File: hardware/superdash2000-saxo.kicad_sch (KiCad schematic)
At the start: 8 parts, among them J1 Molex 34691-0161, U1 L7805

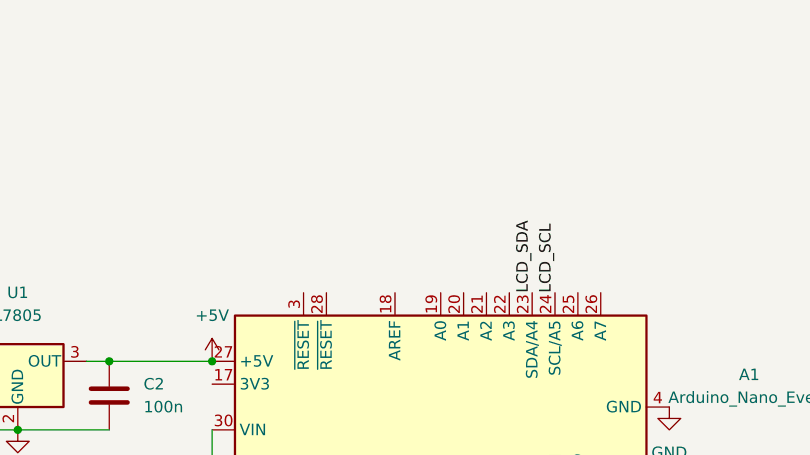
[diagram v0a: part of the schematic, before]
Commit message: hardware: Add voltage divider for battery measurement
Signed-off-by: Thomas Antonini <antonini.thomas@gmail.com>
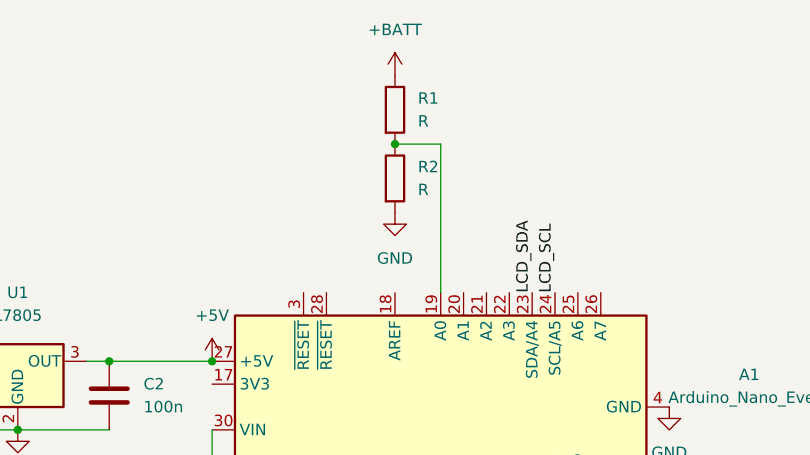
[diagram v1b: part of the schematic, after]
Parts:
- added R1, R2: R, symbol Device:R
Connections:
- net +BATT: now also R1.1
- net GND: now also R2.2
- net at A1.19 (A0): now also R1.2, R2.1
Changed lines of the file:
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@@
   (junction (at 123.19 58.42) (diameter 0) (color 0 0 0 0)
   )
+  (junction (at 154.94 34.29) (diameter 0) (color 0 0 0 0)
+  )
   (junction (at 113.03 66.04) (diameter 0) (color 0 0 0 0)
   )
@@
     (stroke (width 0) (type default) (color 0 0 0 0))
   )
+  (wire (pts (xy 160.02 34.29) (xy 154.94 34.29))
+    (stroke (width 0) (type default) (color 0 0 0 0))
+  )
   (wire (pts (xy 134.62 66.04) (xy 134.62 74.93))
     (stroke (width 0) (type default) (color 0 0 0 0))
@@
   )
   (wire (pts (xy 87.63 71.12) (xy 87.63 74.93))
+    (stroke (width 0) (type default) (color 0 0 0 0))
+  )
+  (wire (pts (xy 160.02 50.8) (xy 160.02 34.29))
     (stroke (width 0) (type default) (color 0 0 0 0))
   )
@@
     )
     (property "Datasheet" "" (id 3) (at 38.1 64.77 0)
+      (effects (font (size 1.27 1.27)) hide)
+    )
+    (pin "1")
+  )
+  (symbol (lib_name "GND_1") (lib_id "power:GND") (at 154.94 41.91 0) (unit 1)
+    (in_bom yes) (on_board yes) (fields_autoplaced)
+    (property "Reference" "#PWR?" (id 0) (at 154.94 48.26 0)
+      (effects (font (size 1.27 1.27)) hide)
+    )
+    (property "Value" "GND" (id 1) (at 154.94 46.99 0))
+    (property "Footprint" "" (id 2) (at 154.94 41.91 0)
+      (effects (font (size 1.27 1.27)) hide)
+    )
+    (property "Datasheet" "" (id 3) (at 154.94 41.91 0)
       (effects (font (size 1.27 1.27)) hide)
     )
@@
     (pin "3")
   )
+  (symbol (lib_id "power:+BATT") (at 154.94 26.67 0) (unit 1)
+    (in_bom yes) (on_board yes) (fields_autoplaced)
+    (property "Reference" "#PWR1" (id 0) (at 154.94 30.48 0)
+      (effects (font (size 1.27 1.27)) hide)
+    )
+    (property "Value" "+BATT" (id 1) (at 154.94 21.59 0))
+    (property "Footprint" "" (id 2) (at 154.94 26.67 0)
+      (effects (font (size 1.27 1.27)) hide)
+    )
+    (property "Datasheet" "" (id 3) (at 154.94 26.67 0)
+      (effects (font (size 1.27 1.27)) hide)
+    )
+    (pin "1")
+  )
   (symbol (lib_id "power:+BATT") (at 81.28 64.77 0) (unit 1)
     (in_bom yes) (on_board yes) (fields_autoplaced)
@@
     (pin "2")
   )
+  (symbol (lib_id "Device:R") (at 154.94 30.48 0) (unit 1)
+    (in_bom yes) (on_board yes) (fields_autoplaced)
+    (property "Reference" "R1" (id 0) (at 157.48 29.2099 0)
+      (effects (font (size 1.27 1.27)) (justify left))
+    )
+    (property "Value" "R" (id 1) (at 157.48 31.7499 0)
+      (effects (font (size 1.27 1.27)) (justify left))
+    )
+    (property "Footprint" "" (id 2) (at 153.162 30.48 90)
+      (effects (font (size 1.27 1.27)) hide)
+    )
+    (property "Datasheet" "~" (id 3) (at 154.94 30.48 0)
+      (effects (font (size 1.27 1.27)) hide)
+    )
+    (pin "1")
+    (pin "2")
+  )
+  (symbol (lib_id "Device:R") (at 154.94 38.1 0) (unit 1)
+    (in_bom yes) (on_board yes) (fields_autoplaced)
+    (property "Reference" "R2" (id 0) (at 157.48 36.8299 0)
+      (effects (font (size 1.27 1.27)) (justify left))
+    )
+    (property "Value" "R" (id 1) (at 157.48 39.3699 0)
+      (effects (font (size 1.27 1.27)) (justify left))
+    )
+    (property "Footprint" "" (id 2) (at 153.162 38.1 90)
+      (effects (font (size 1.27 1.27)) hide)
+    )
+    (property "Datasheet" "~" (id 3) (at 154.94 38.1 0)
+      (effects (font (size 1.27 1.27)) hide)
+    )
+    (pin "1")
+    (pin "2")
+  )
   (sheet_instances
     (path "/" (page "1"))
   )
   (symbol_instances
+    (path "/b87c930c-8d22-4000-a82f-ac742bad5f6a"
+      (reference "#PWR1") (unit 1) (value "+BATT") (footprint "")
+    )
     (path "/bfcc77a0-ee67-4af0-9e4b-c64f7ccc8208"
       (reference "#PWR1") (unit 1) (value "+BATT") (footprint "")
@@
       (reference "#PWR0106") (unit 1) (value "GND") (footprint "")
     )
+    (path "/2c2c0160-d229-41a2-b822-4cf1420ec8e9"
+      (reference "#PWR?") (unit 1) (value "GND") (footprint "")
+    )
     (path "/65c02b6a-4170-4a63-9193-eec01920d5e8"
       (reference "A1") (unit 1) (value "Arduino_Nano_Every") (footprint "Module:Arduino_Nano")
@@
       (reference "JP1") (unit 1) (value "Jumper_3_Bridged12") (footprint "")
     )
+    (path "/f89ebb12-89cc-4956-9979-cdeb115f9256"
+      (reference "R1") (unit 1) (value "R") (footprint "")
+    )
+    (path "/fece9861-2ca2-4e20-aacd-7057d18618e8"
+      (reference "R2") (unit 1) (value "R") (footprint "")
+    )
     (path "/8f188f22-a5b9-4f36-a20f-c9a07bb49266"

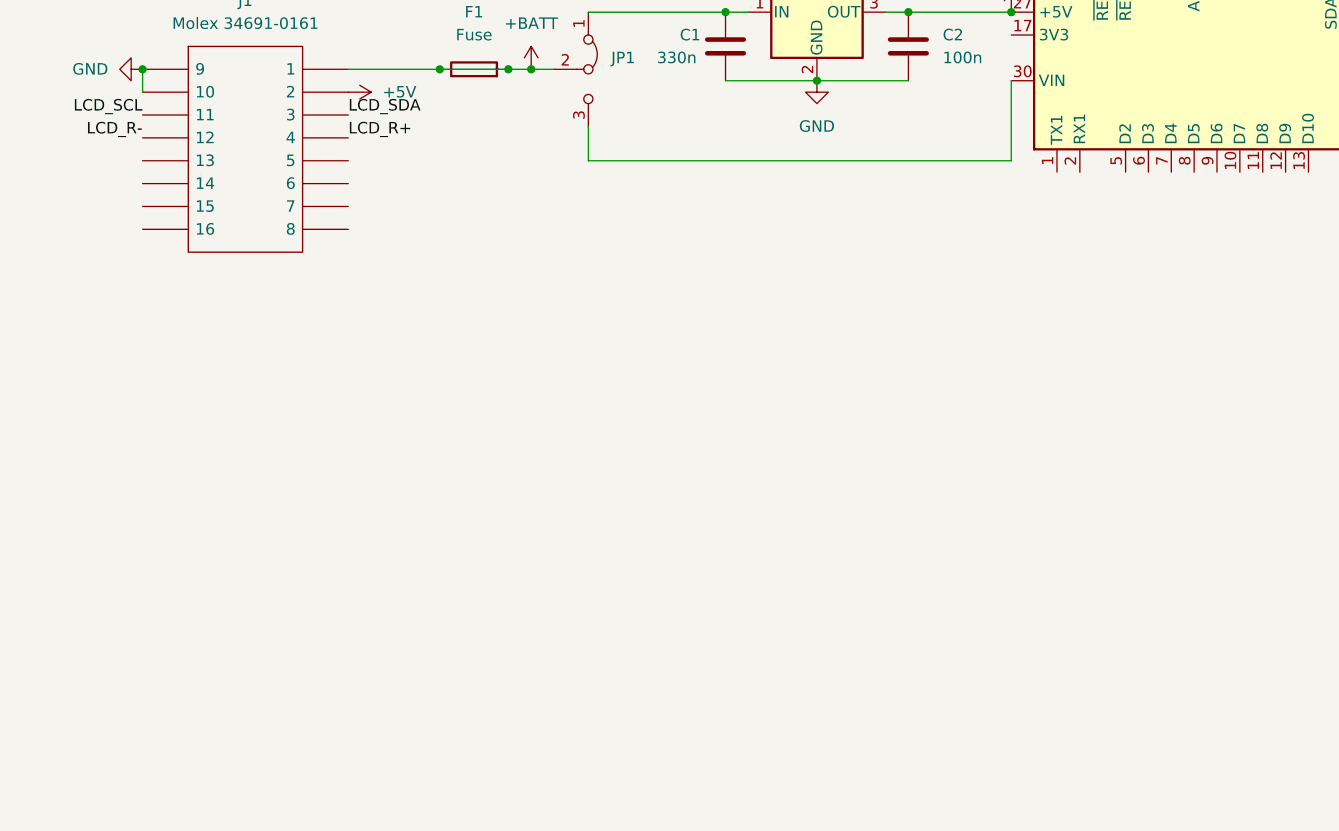
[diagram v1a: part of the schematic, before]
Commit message: hardware: Add water temp signal with opamp + voltage divider
Signed-off-by: Thomas Antonini <antonini.thomas@gmail.com>
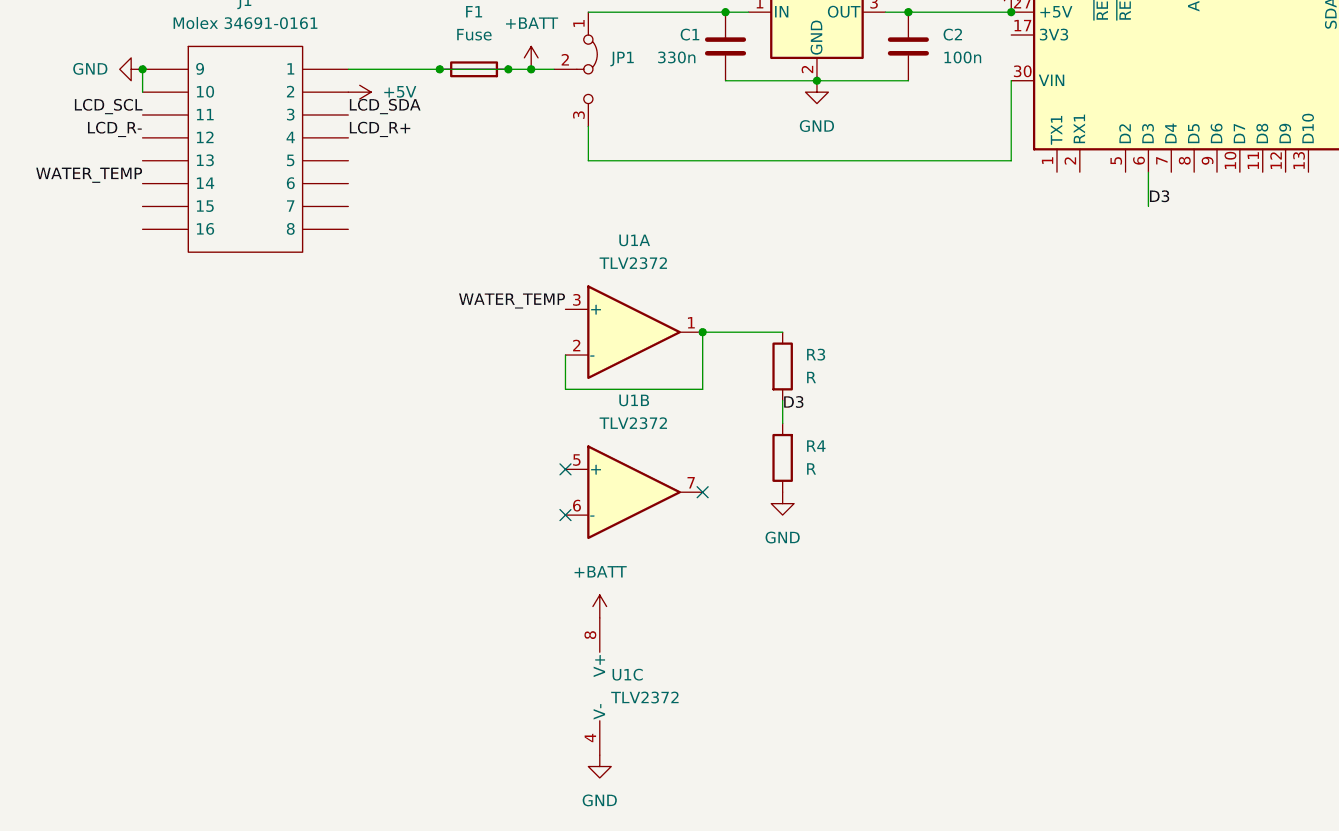
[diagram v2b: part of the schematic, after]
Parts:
- added R3, R4: R, symbol Device:R
- added unit 3 of U1
- added unit 2 of U1
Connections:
- net +BATT: now also U1.8 (V+)
- net GND: now also R4.1, U1.4 (V-)
- net D3: now reaches A1.6 (D3)
- net D3: now also R3.2, R4.2
- net WATER_TEMP: now reaches J1.14
- net WATER_TEMP: now also U1.3 (+)
- new net: R3.1, U1.1, U1.2 (-)
- no-connect marks 0 -> 3
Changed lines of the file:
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@@
   (junction (at 134.62 58.42) (diameter 0) (color 0 0 0 0)
   )
+  (junction (at 100.33 93.98) (diameter 0) (color 0 0 0 0)
+  )
   (junction (at 123.19 58.42) (diameter 0) (color 0 0 0 0)
   )
@@
   (junction (at 78.74 64.77) (diameter 0) (color 0 0 0 0)
   )
+  (no_connect (at 85.09 109.22))
+  (no_connect (at 85.09 114.3))
+  (no_connect (at 100.33 111.76))
   (wire (pts (xy 134.62 74.93) (xy 87.63 74.93))
     (stroke (width 0) (type default) (color 0 0 0 0))
@@
     (stroke (width 0) (type default) (color 0 0 0 0))
   )
+  (wire (pts (xy 85.09 100.33) (xy 100.33 100.33))
+    (stroke (width 0) (type default) (color 0 0 0 0))
+  )
+  (wire (pts (xy 85.09 96.52) (xy 85.09 100.33))
+    (stroke (width 0) (type default) (color 0 0 0 0))
+  )
+  (wire (pts (xy 149.86 76.2) (xy 149.86 80.01))
+    (stroke (width 0) (type default) (color 0 0 0 0))
+  )
+  (wire (pts (xy 100.33 93.98) (xy 100.33 100.33))
+    (stroke (width 0) (type default) (color 0 0 0 0))
+  )
   (wire (pts (xy 113.03 66.04) (xy 123.19 66.04))
     (stroke (width 0) (type default) (color 0 0 0 0))
@@
     (stroke (width 0) (type default) (color 0 0 0 0))
   )
+  (wire (pts (xy 100.33 93.98) (xy 109.22 93.98))
+    (stroke (width 0) (type default) (color 0 0 0 0))
+  )
   (wire (pts (xy 81.28 64.77) (xy 83.82 64.77))
     (stroke (width 0) (type default) (color 0 0 0 0))
   )
+  (wire (pts (xy 109.22 101.6) (xy 109.22 104.14))
+    (stroke (width 0) (type default) (color 0 0 0 0))
+  )
   (wire (pts (xy 102.87 58.42) (xy 105.41 58.42))
     (stroke (width 0) (type default) (color 0 0 0 0))
@@
     (effects (font (size 1.27 1.27)) (justify left bottom))
   )
+  (label "WATER_TEMP" (at 38.1 77.47 180)
+    (effects (font (size 1.27 1.27)) (justify right bottom))
+  )
   (label "LCD_R+" (at 229.87 55.88 0)
     (effects (font (size 1.27 1.27)) (justify left bottom))
@@
   (label "LCD_SDA" (at 60.96 69.85 0)
     (effects (font (size 1.27 1.27)) (justify left bottom))
+  )
+  (label "WATER_TEMP" (at 85.09 91.44 180)
+    (effects (font (size 1.27 1.27)) (justify right bottom))
   )
   (label "LCD_SCL" (at 38.1 69.85 180)
@@
     (effects (font (size 1.27 1.27)) (justify right bottom))
   )
+  (label "D3" (at 109.22 102.87 0)
+    (effects (font (size 1.27 1.27)) (justify left bottom))
+  )
   (label "LCD_SCL" (at 172.72 50.8 90)
+    (effects (font (size 1.27 1.27)) (justify left bottom))
+  )
+  (label "D3" (at 149.86 80.01 0)
     (effects (font (size 1.27 1.27)) (justify left bottom))
   )
@@
     (pin "2")
   )
+  (symbol (lib_id "Amplifier_Operational:TLV2372") (at 91.44 133.35 0) (unit 3)
+    (in_bom yes) (on_board yes) (fields_autoplaced)
+    (property "Reference" "U1" (id 0) (at 90.17 132.0799 0)
+      (effects (font (size 1.27 1.27)) (justify left))
+    )
+    (property "Value" "TLV2372" (id 1) (at 90.17 134.6199 0)
+      (effects (font (size 1.27 1.27)) (justify left))
+    )
+    (property "Footprint" "" (id 2) (at 91.44 133.35 0)
+      (effects (font (size 1.27 1.27)) hide)
+    )
+    (property "Datasheet" "http://www.ti.com/lit/ds/symlink/tlv2375.pdf" (id 3) (at 91.44 133.35 0)
+      (effects (font (size 1.27 1.27)) hide)
+    )
+    (pin "1")
+    (pin "2")
+    (pin "3")
+    (pin "5")
+    (pin "6")
+    (pin "7")
+    (pin "4")
+    (pin "8")
+  )
   (symbol (lib_id "Jumper:Jumper_3_Bridged12") (at 87.63 64.77 270) (unit 1)
     (in_bom yes) (on_board yes)
@@
     (pin "1")
     (pin "2")
+  )
+  (symbol (lib_name "GND_3") (lib_id "power:GND") (at 109.22 111.76 0) (unit 1)
+    (in_bom yes) (on_board yes) (fields_autoplaced)
+    (property "Reference" "#PWR?" (id 0) (at 109.22 118.11 0)
+      (effects (font (size 1.27 1.27)) hide)
+    )
+    (property "Value" "GND" (id 1) (at 109.22 116.84 0))
+    (property "Footprint" "" (id 2) (at 109.22 111.76 0)
+      (effects (font (size 1.27 1.27)) hide)
+    )
+    (property "Datasheet" "" (id 3) (at 109.22 111.76 0)
+      (effects (font (size 1.27 1.27)) hide)
+    )
+    (pin "1")
   )
   (symbol (lib_id "Regulator_Linear:L7805") (at 113.03 58.42 0) (unit 1)
@@
     (pin "9")
   )
+  (symbol (lib_id "Device:R") (at 109.22 107.95 180) (unit 1)
+    (in_bom yes) (on_board yes) (fields_autoplaced)
+    (property "Reference" "R4" (id 0) (at 111.76 106.6799 0)
+      (effects (font (size 1.27 1.27)) (justify right))
+    )
+    (property "Value" "R" (id 1) (at 111.76 109.2199 0)
+      (effects (font (size 1.27 1.27)) (justify right))
+    )
+    (property "Footprint" "" (id 2) (at 110.998 107.95 90)
+      (effects (font (size 1.27 1.27)) hide)
+    )
+    (property "Datasheet" "~" (id 3) (at 109.22 107.95 0)
+      (effects (font (size 1.27 1.27)) hide)
+    )
+    (pin "1")
+    (pin "2")
+  )
   (symbol (lib_id "Molex_34691-0161:Molex 34691-0161") (at 38.1 64.77 0) (unit 1)
     (in_bom yes) (on_board yes) (fields_autoplaced)
@@
     (pin "3")
   )
+  (symbol (lib_name "GND_2") (lib_id "power:GND") (at 88.9 140.97 0) (unit 1)
+    (in_bom yes) (on_board yes) (fields_autoplaced)
+    (property "Reference" "#PWR?" (id 0) (at 88.9 147.32 0)
+      (effects (font (size 1.27 1.27)) hide)
+    )
+    (property "Value" "GND" (id 1) (at 88.9 146.05 0))
+    (property "Footprint" "" (id 2) (at 88.9 140.97 0)
+      (effects (font (size 1.27 1.27)) hide)
+    )
+    (property "Datasheet" "" (id 3) (at 88.9 140.97 0)
+      (effects (font (size 1.27 1.27)) hide)
+    )
+    (pin "1")
+  )
   (symbol (lib_id "power:+BATT") (at 154.94 26.67 0) (unit 1)
     (in_bom yes) (on_board yes) (fields_autoplaced)
@@
     )
     (pin "1")
+  )
+  (symbol (lib_id "power:+BATT") (at 88.9 125.73 0) (unit 1)
+    (in_bom yes) (on_board yes) (fields_autoplaced)
+    (property "Reference" "#PWR?" (id 0) (at 88.9 129.54 0)
+      (effects (font (size 1.27 1.27)) hide)
+    )
+    (property "Value" "+BATT" (id 1) (at 88.9 120.65 0))
+    (property "Footprint" "" (id 2) (at 88.9 125.73 0)
+      (effects (font (size 1.27 1.27)) hide)
+    )
+    (property "Datasheet" "" (id 3) (at 88.9 125.73 0)
+      (effects (font (size 1.27 1.27)) hide)
+    )
+    (pin "1")
+  )
+  (symbol (lib_id "Amplifier_Operational:TLV2372") (at 92.71 93.98 0) (unit 1)
+    (in_bom yes) (on_board yes) (fields_autoplaced)
+    (property "Reference" "U1" (id 0) (at 92.71 83.82 0))
+    (property "Value" "TLV2372" (id 1) (at 92.71 86.36 0))
+    (property "Footprint" "" (id 2) (at 92.71 93.98 0)
+      (effects (font (size 1.27 1.27)) hide)
+    )
+    (property "Datasheet" "http://www.ti.com/lit/ds/symlink/tlv2375.pdf" (id 3) (at 92.71 93.98 0)
+      (effects (font (size 1.27 1.27)) hide)
+    )
+    (pin "1")
+    (pin "2")
+    (pin "3")
+    (pin "5")
+    (pin "6")
+    (pin "7")
+    (pin "4")
+    (pin "8")
+  )
+  (symbol (lib_id "Amplifier_Operational:TLV2372") (at 92.71 111.76 0) (unit 2)
+    (in_bom yes) (on_board yes) (fields_autoplaced)
+    (property "Reference" "U1" (id 0) (at 92.71 101.6 0))
+    (property "Value" "TLV2372" (id 1) (at 92.71 104.14 0))
+    (property "Footprint" "" (id 2) (at 92.71 111.76 0)
+      (effects (font (size 1.27 1.27)) hide)
+    )
+    (property "Datasheet" "http://www.ti.com/lit/ds/symlink/tlv2375.pdf" (id 3) (at 92.71 111.76 0)
+      (effects (font (size 1.27 1.27)) hide)
+    )
+    (pin "1")
+    (pin "2")
+    (pin "3")
+    (pin "5")
+    (pin "6")
+    (pin "7")
+    (pin "4")
+    (pin "8")
   )
   (symbol (lib_id "Device:C") (at 102.87 62.23 0) (unit 1)
@@
     (pin "2")
   )
+  (symbol (lib_id "Device:R") (at 109.22 97.79 0) (unit 1)
+    (in_bom yes) (on_board yes) (fields_autoplaced)
+    (property "Reference" "R3" (id 0) (at 111.76 96.5199 0)
+      (effects (font (size 1.27 1.27)) (justify left))
+    )
+    (property "Value" "R" (id 1) (at 111.76 99.0599 0)
+      (effects (font (size 1.27 1.27)) (justify left))
+    )
+    (property "Footprint" "" (id 2) (at 107.442 97.79 90)
+      (effects (font (size 1.27 1.27)) hide)
+    )
+    (property "Datasheet" "~" (id 3) (at 109.22 97.79 0)
+      (effects (font (size 1.27 1.27)) hide)
+    )
+    (pin "1")
+    (pin "2")
+  )
   (symbol (lib_id "Device:R") (at 154.94 30.48 0) (unit 1)
     (in_bom yes) (on_board yes) (fields_autoplaced)
@@
       (reference "#PWR?") (unit 1) (value "GND") (footprint "")
     )
+    (path "/44a14783-b732-4cad-b4e3-6acdd52fd22f"
+      (reference "#PWR?") (unit 1) (value "GND") (footprint "")
+    )
+    (path "/a55a6c63-efeb-4a39-b005-db7246ff05b2"
+      (reference "#PWR?") (unit 1) (value "GND") (footprint "")
+    )
+    (path "/dca402e7-0e77-45e9-a01b-7f7133721d95"
+      (reference "#PWR?") (unit 1) (value "+BATT") (footprint "")
+    )
     (path "/65c02b6a-4170-4a63-9193-eec01920d5e8"
       (reference "A1") (unit 1) (value "Arduino_Nano_Every") (footprint "Module:Arduino_Nano")
@@
       (reference "R2") (unit 1) (value "R") (footprint "")
     )
+    (path "/f15081b0-7cf7-4fce-a8fa-54b8b1f48d70"
+      (reference "R3") (unit 1) (value "R") (footprint "")
+    )
+    (path "/6c35ba2a-d207-4d6a-b21b-53599f947c95"
+      (reference "R4") (unit 1) (value "R") (footprint "")
+    )
     (path "/8f188f22-a5b9-4f36-a20f-c9a07bb49266"
       (reference "RV1") (unit 1) (value "R_Potentiometer") (footprint "")
@@
       (reference "U1") (unit 1) (value "L7805") (footprint "Package_TO_SOT_THT:TO-220-3_Vertical")
     )
-  )
+    (path "/dd5c3b2c-bf9a-4210-9e80-91b487d16ffc"
+      (reference "U1") (unit 1) (value "TLV2372") (footprint "")
+    )
+    (path "/decc528c-3d97-4a7b-9669-34ab28ca3491"
+      (reference "U1") (unit 2) (value "TLV2372") (footprint "")
+    )
+    (path "/37d731ac-aa73-4d1a-b688-0abbd56fee75"
+      (reference "U1") (unit 3) (value "TLV2372") (footprint "")
+    )
+  )
